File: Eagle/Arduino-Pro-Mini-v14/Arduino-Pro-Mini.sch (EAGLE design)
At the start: 15 parts, among them Q1 8/16/20MHz, U1 ATMEGA328, U2 MIC5205

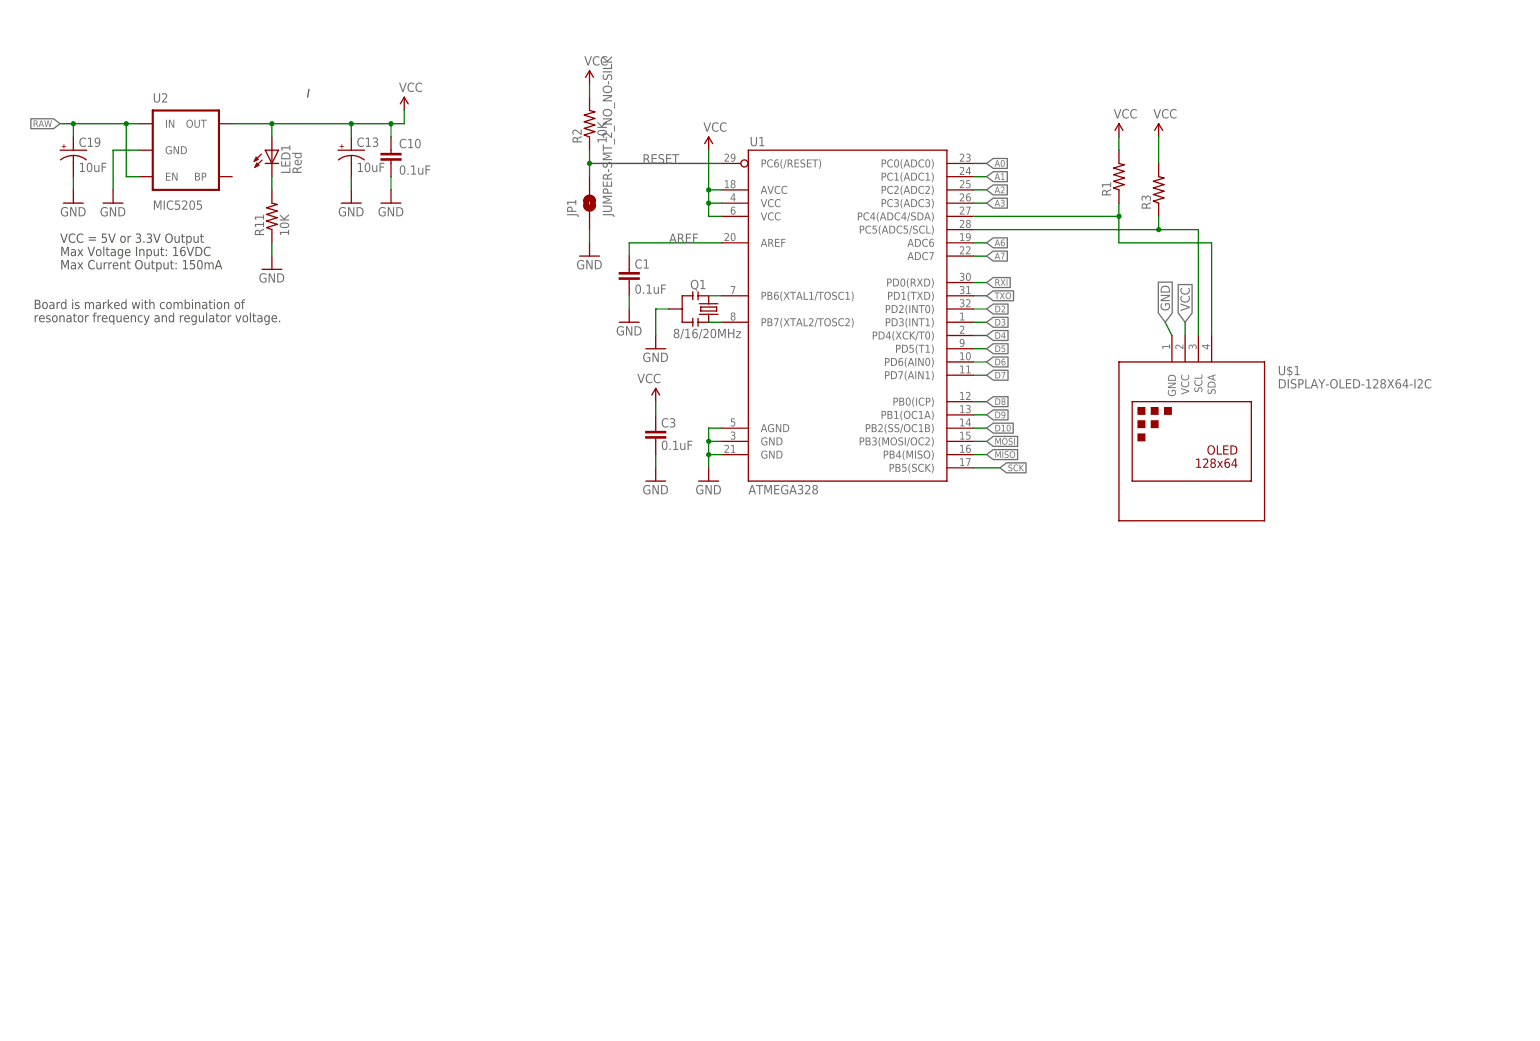
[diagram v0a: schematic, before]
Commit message: Added LED driers
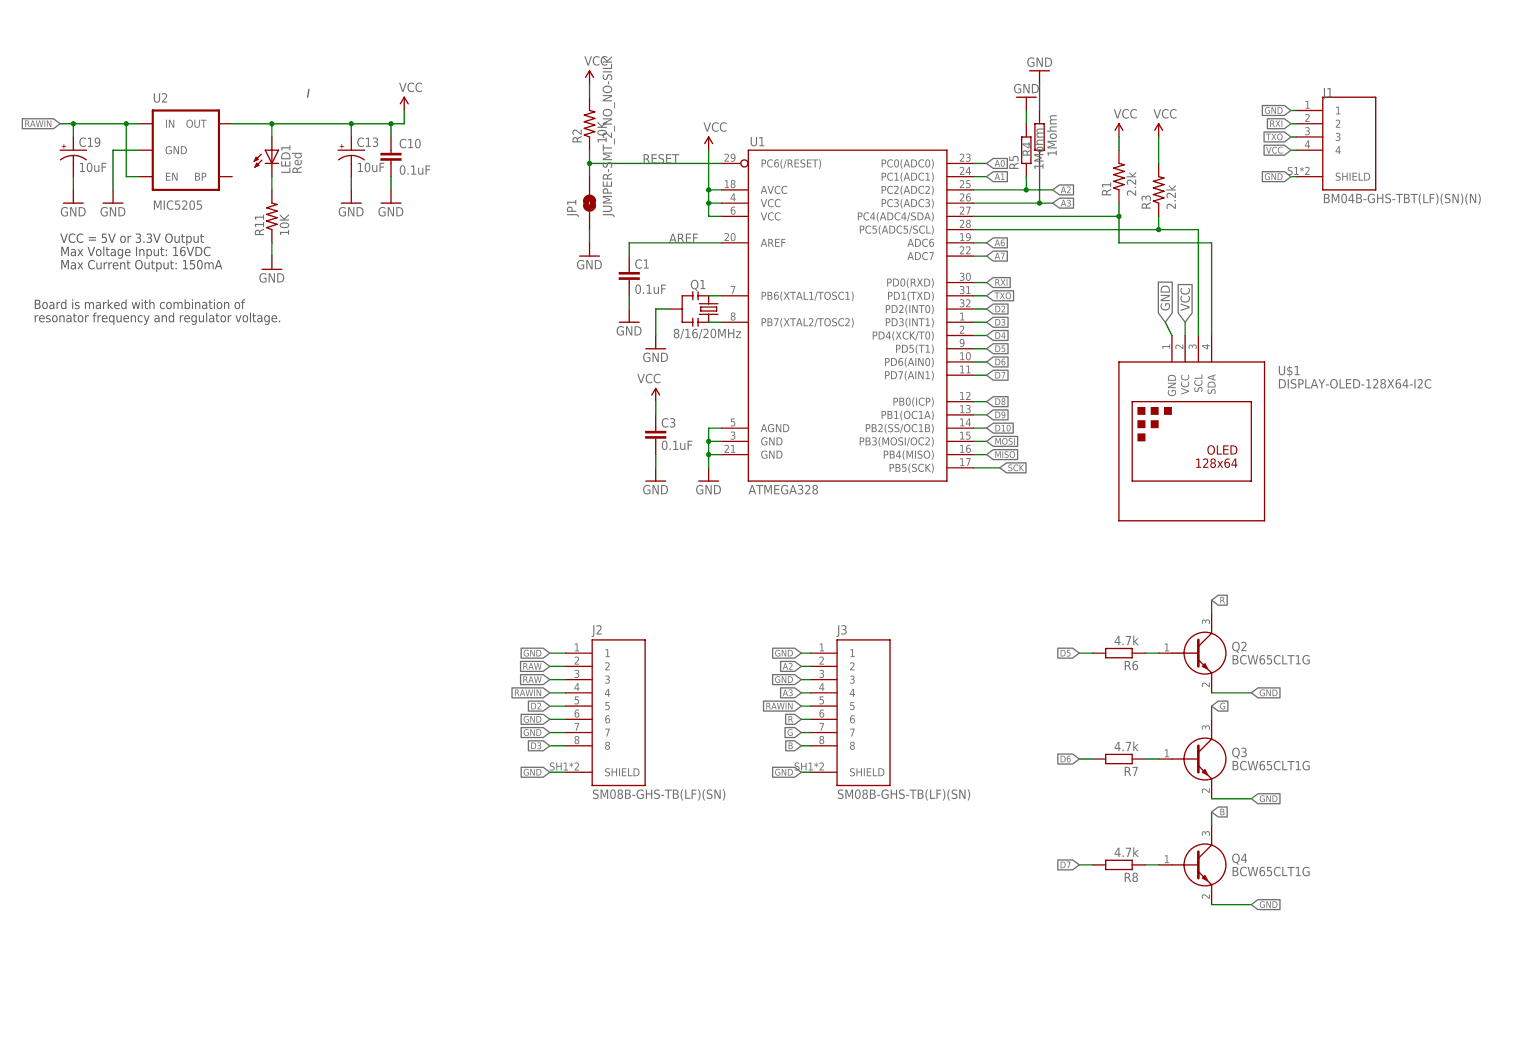
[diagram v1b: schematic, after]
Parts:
- added J1: BM04B-GHS-TBT(LF)(SN)(N), BM04B-GHS-TBT_LF__SN__N_:BM04B-GHS-TBT(LF)(SN)(N)
- added J2, J3: SM08B-GHS-TB(LF)(SN), SM08B-GHS-TB_LF__SN_:SM08B-GHS-TB(LF)(SN)
- added Q2, Q3, Q4: BCW65CLT1G, BCW65CLT1G:BCW65CLT1G
- added R4, R5: 1Mohm, eagle-ltspice:RR0402
- added R6, R7, R8: 4.7k, eagle-ltspice:RR0402
- R1, R3: value (none) -> 2.2k
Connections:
- new net B: J3.8, Q4.C
- new net G: J3.7, Q3.C
- new net N$3: Q4.B, R8.1
- new net N$5: Q3.B, R7.1
- new net N$6: Q2.B, R6.1
- new net R: J3.6, Q2.C
- new net RAWIN: C19.+, J2.4, J3.5, U2.EN, U2.IN
- net A2: now also J3.2, R5.1
- net A3: now also J3.4, R4.1
- net D2: now also J2.5
- net D3: now also J2.8
- net D5: now also R6.2
- net D6: now also R7.2
- net D7: now also R8.2
- net GND: now also J1.1, J1.SHIELD, J2.1, J2.6, J2.7, J2.SHIELD, J3.1, J3.3, J3.SHIELD, Q2.E, Q3.E, Q4.E, R4.2, R5.2
- net RAW: now also J2.2, J2.3; no longer C19.+, U2.EN, U2.IN
- net RXI: now also J1.2
- net TXO: now also J1.3
- net VCC: now also J1.4

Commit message: things
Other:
- note removed: "Board is marked with combination of"
- note removed: "Max Current Output: 150mA"
- note removed: "Max Voltage Input: 16VDC"
- note removed: "VCC = 5V or 3.3V Output"
- note removed: "resonator frequency and regulator voltage."
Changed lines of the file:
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@@
 <?xml version="1.0" encoding="utf-8"?>
 <!DOCTYPE eagle SYSTEM "eagle.dtd">
-<eagle version="9.2.2">
+<eagle version="9.5.1">
 <drawing>
 <settings>
@@
 <sheet>
 <plain>
-<text x="20.32" y="137.16" size="1.778" layer="97">Max Voltage Input: 16VDC</text>
-<text x="20.32" y="134.62" size="1.778" layer="97">Max Current Output: 150mA</text>
-<text x="15.24" y="127" size="1.778" layer="97">Board is marked with combination of</text>
-<text x="15.24" y="124.46" size="1.778" layer="97">resonator frequency and regulator voltage.</text>
-<text x="20.32" y="139.7" size="1.778" layer="97">VCC = 5V or 3.3V Output</text>
 <wire x1="67.818" y1="167.64" x2="68.072" y2="169.164" width="0.2032" layer="97"/>
 </plain>

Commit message: Auto stash before merge of "master" and "origin/master"
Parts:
- added R10, R12, R13, R9: 10ohm, eagle-ltspice:RR0402
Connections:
- new net N$7: Q4.C, R9.2
- new net N$8: Q3.C, R10.2
- new net N$9: Q2.C, R12.2
- net AREF: now also R13.2
- net B: now also R9.1; no longer Q4.C
- net G: now also R10.1; no longer Q3.C
- net R: now also R12.1; no longer Q2.C
- net VCC: now also R13.1
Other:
- moved on the sheet: Q3, Q4, R7, R8
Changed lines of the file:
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@@
 <part name="R7" library="eagle-ltspice" library_urn="urn:adsk.eagle:library:217" deviceset="R" device="R0402" package3d_urn="urn:adsk.eagle:package:13296/1" value="4.7k"/>
 <part name="R8" library="eagle-ltspice" library_urn="urn:adsk.eagle:library:217" deviceset="R" device="R0402" package3d_urn="urn:adsk.eagle:package:13296/1" value="4.7k"/>
+<part name="R9" library="eagle-ltspice" library_urn="urn:adsk.eagle:library:217" deviceset="R" device="R0402" package3d_urn="urn:adsk.eagle:package:13296/1" value="10ohm"/>
+<part name="R10" library="eagle-ltspice" library_urn="urn:adsk.eagle:library:217" deviceset="R" device="R0402" package3d_urn="urn:adsk.eagle:package:13296/1" value="10ohm"/>
+<part name="R12" library="eagle-ltspice" library_urn="urn:adsk.eagle:library:217" deviceset="R" device="R0402" package3d_urn="urn:adsk.eagle:package:13296/1" value="10ohm"/>
+<part name="R13" library="eagle-ltspice" library_urn="urn:adsk.eagle:library:217" deviceset="R" device="R0402" package3d_urn="urn:adsk.eagle:package:13296/1" value="10ohm"/>
 </parts>
 <sheets>
@@
 <attribute name="VALUE" x="245.11" y="59.69" size="1.778" layer="96" align="center-left"/>
 </instance>
-<instance part="Q3" gate="G$1" x="231.14" y="40.64" smashed="yes">
-<attribute name="NAME" x="245.11" y="41.91" size="1.778" layer="95" align="center-left"/>
-<attribute name="VALUE" x="245.11" y="39.37" size="1.778" layer="96" align="center-left"/>
-</instance>
-<instance part="Q4" gate="G$1" x="231.14" y="20.32" smashed="yes">
-<attribute name="NAME" x="245.11" y="21.59" size="1.778" layer="95" align="center-left"/>
-<attribute name="VALUE" x="245.11" y="19.05" size="1.778" layer="96" align="center-left"/>
+<instance part="Q3" gate="G$1" x="231.14" y="27.94" smashed="yes">
+<attribute name="NAME" x="245.11" y="29.21" size="1.778" layer="95" align="center-left"/>
+<attribute name="VALUE" x="245.11" y="26.67" size="1.778" layer="96" align="center-left"/>
+</instance>
+<instance part="Q4" gate="G$1" x="231.14" y="-2.54" smashed="yes">
+<attribute name="NAME" x="245.11" y="-1.27" size="1.778" layer="95" align="center-left"/>
+<attribute name="VALUE" x="245.11" y="-3.81" size="1.778" layer="96" align="center-left"/>
 </instance>
 <instance part="R6" gate="G$1" x="223.52" y="60.96" smashed="yes" rot="R180">
@@
 <attribute name="VALUE" x="227.33" y="64.262" size="1.778" layer="96" rot="R180"/>
 </instance>
-<instance part="R7" gate="G$1" x="223.52" y="40.64" smashed="yes" rot="R180">
-<attribute name="NAME" x="227.33" y="39.1414" size="1.778" layer="95" rot="R180"/>
-<attribute name="VALUE" x="227.33" y="43.942" size="1.778" layer="96" rot="R180"/>
-</instance>
-<instance part="R8" gate="G$1" x="223.52" y="20.32" smashed="yes" rot="R180">
-<attribute name="NAME" x="227.33" y="18.8214" size="1.778" layer="95" rot="R180"/>
-<attribute name="VALUE" x="227.33" y="23.622" size="1.778" layer="96" rot="R180"/>
+<instance part="R7" gate="G$1" x="223.52" y="27.94" smashed="yes" rot="R180">
+<attribute name="NAME" x="227.33" y="26.4414" size="1.778" layer="95" rot="R180"/>
+<attribute name="VALUE" x="227.33" y="31.242" size="1.778" layer="96" rot="R180"/>
+</instance>
+<instance part="R8" gate="G$1" x="223.52" y="-2.54" smashed="yes" rot="R180">
+<attribute name="NAME" x="227.33" y="-4.0386" size="1.778" layer="95" rot="R180"/>
+<attribute name="VALUE" x="227.33" y="0.762" size="1.778" layer="96" rot="R180"/>
+</instance>
+<instance part="R9" gate="G$1" x="241.3" y="10.16" smashed="yes" rot="R270">
+<attribute name="NAME" x="242.7986" y="13.97" size="1.778" layer="95" rot="R270"/>
+<attribute name="VALUE" x="237.998" y="13.97" size="1.778" layer="96" rot="R270"/>
+</instance>
+<instance part="R10" gate="G$1" x="241.3" y="40.64" smashed="yes" rot="R270">
+<attribute name="NAME" x="242.7986" y="44.45" size="1.778" layer="95" rot="R270"/>
+<attribute name="VALUE" x="237.998" y="44.45" size="1.778" layer="96" rot="R270"/>
+</instance>
+<instance part="R12" gate="G$1" x="241.3" y="73.66" smashed="yes" rot="R270">
+<attribute name="NAME" x="242.7986" y="77.47" size="1.778" layer="95" rot="R270"/>
+<attribute name="VALUE" x="237.998" y="77.47" size="1.778" layer="96" rot="R270"/>
+</instance>
+<instance part="R13" gate="G$1" x="134.62" y="144.78" smashed="yes" rot="R270">
+<attribute name="NAME" x="136.1186" y="148.59" size="1.778" layer="95" rot="R270"/>
+<attribute name="VALUE" x="131.318" y="148.59" size="1.778" layer="96" rot="R270"/>
 </instance>
 </instances>
@@
 <segment>
 <pinref part="Q3" gate="G$1" pin="E"/>
-<wire x1="241.3" y1="33.02" x2="248.92" y2="33.02" width="0.1524" layer="91"/>
-<label x="248.92" y="33.02" size="1.27" layer="95" xref="yes"/>
+<wire x1="241.3" y1="20.32" x2="248.92" y2="20.32" width="0.1524" layer="91"/>
+<label x="248.92" y="20.32" size="1.27" layer="95" xref="yes"/>
 </segment>
 <segment>
 <pinref part="Q4" gate="G$1" pin="E"/>
-<wire x1="241.3" y1="12.7" x2="248.92" y2="12.7" width="0.1524" layer="91"/>
-<label x="248.92" y="12.7" size="1.27" layer="95" xref="yes"/>
+<wire x1="241.3" y1="-10.16" x2="248.92" y2="-10.16" width="0.1524" layer="91"/>
+<label x="248.92" y="-10.16" size="1.27" layer="95" xref="yes"/>
 </segment>
 </net>
 <net name="AREF" class="0">
 <segment>
-<wire x1="147.32" y1="139.7" x2="129.54" y2="139.7" width="0.1524" layer="91"/>
+<wire x1="147.32" y1="139.7" x2="134.62" y2="139.7" width="0.1524" layer="91"/>
+<wire x1="134.62" y1="139.7" x2="129.54" y2="139.7" width="0.1524" layer="91"/>
 <wire x1="129.54" y1="139.7" x2="129.54" y2="137.16" width="0.1524" layer="91"/>
 <label x="137.16" y="139.7" size="1.778" layer="95"/>
 <pinref part="C1" gate="G$1" pin="2"/>
 <pinref part="U1" gate="G$1" pin="AREF"/>
+<pinref part="R13" gate="G$1" pin="2"/>
+<junction x="134.62" y="139.7"/>
 </segment>
 </net>
@@
 <segment>
 <wire x1="147.32" y1="149.86" x2="144.78" y2="149.86" width="0.1524" layer="91"/>
-<wire x1="144.78" y1="149.86" x2="144.78" y2="157.48" width="0.1524" layer="91"/>
+<wire x1="144.78" y1="149.86" x2="144.78" y2="152.4" width="0.1524" layer="91"/>
+<wire x1="144.78" y1="152.4" x2="144.78" y2="157.48" width="0.1524" layer="91"/>
 <wire x1="147.32" y1="147.32" x2="144.78" y2="147.32" width="0.1524" layer="91"/>
 <wire x1="144.78" y1="147.32" x2="144.78" y2="149.86" width="0.1524" layer="91"/>
@@
 <pinref part="U1" gate="G$1" pin="VCC@2"/>
 <pinref part="P+1" gate="G$1" pin="3.3V"/>
+<pinref part="R13" gate="G$1" pin="1"/>
+<wire x1="134.62" y1="149.86" x2="134.62" y2="152.4" width="0.1524" layer="91"/>
+<wire x1="134.62" y1="152.4" x2="144.78" y2="152.4" width="0.1524" layer="91"/>
+<junction x="144.78" y="152.4"/>
 </segment>
 <segment>
@@
 <segment>
 <pinref part="R7" gate="G$1" pin="2"/>
-<wire x1="218.44" y1="40.64" x2="215.9" y2="40.64" width="0.1524" layer="91"/>
-<label x="215.9" y="40.64" size="1.27" layer="95" rot="R180" xref="yes"/>
+<wire x1="218.44" y1="27.94" x2="215.9" y2="27.94" width="0.1524" layer="91"/>
+<label x="215.9" y="27.94" size="1.27" layer="95" rot="R180" xref="yes"/>
 </segment>
 </net>
@@
 <segment>
 <pinref part="R8" gate="G$1" pin="2"/>
-<wire x1="218.44" y1="20.32" x2="215.9" y2="20.32" width="0.1524" layer="91"/>
-<label x="215.9" y="20.32" size="1.27" layer="95" rot="R180" xref="yes"/>
+<wire x1="218.44" y1="-2.54" x2="215.9" y2="-2.54" width="0.1524" layer="91"/>
+<label x="215.9" y="-2.54" size="1.27" layer="95" rot="R180" xref="yes"/>
 </segment>
 </net>
@@
 </segment>
 <segment>
-<pinref part="Q4" gate="G$1" pin="C"/>
-<wire x1="241.3" y1="27.94" x2="241.3" y2="30.48" width="0.1524" layer="91"/>
-<label x="241.3" y="30.48" size="1.27" layer="95" xref="yes"/>
+<label x="241.3" y="17.78" size="1.27" layer="95" xref="yes"/>
+<wire x1="241.3" y1="15.24" x2="241.3" y2="17.78" width="0.1524" layer="91"/>
+<pinref part="R9" gate="G$1" pin="1"/>
 </segment>
 </net>
@@
 </segment>
 <segment>
-<pinref part="Q3" gate="G$1" pin="C"/>
-<wire x1="241.3" y1="48.26" x2="241.3" y2="50.8" width="0.1524" layer="91"/>
-<label x="241.3" y="50.8" size="1.27" layer="95" xref="yes"/>
+<label x="241.3" y="48.26" size="1.27" layer="95" xref="yes"/>
+<wire x1="241.3" y1="45.72" x2="241.3" y2="48.26" width="0.1524" layer="91"/>
+<pinref part="R10" gate="G$1" pin="1"/>
 </segment>
 </net>
@@
 </segment>
 <segment>
-<pinref part="Q2" gate="G$1" pin="C"/>
-<wire x1="241.3" y1="68.58" x2="241.3" y2="71.12" width="0.1524" layer="91"/>
-<label x="241.3" y="71.12" size="1.27" layer="95" xref="yes"/>
+<label x="241.3" y="81.28" size="1.27" layer="95" xref="yes"/>
+<pinref part="R12" gate="G$1" pin="1"/>
+<wire x1="241.3" y1="78.74" x2="241.3" y2="81.28" width="0.1524" layer="91"/>
 </segment>
 </net>
@@
 <pinref part="R8" gate="G$1" pin="1"/>
 <pinref part="Q4" gate="G$1" pin="B"/>
-<wire x1="228.6" y1="20.32" x2="231.14" y2="20.32" width="0.1524" layer="91"/>
+<wire x1="228.6" y1="-2.54" x2="231.14" y2="-2.54" width="0.1524" layer="91"/>
 </segment>
 </net>
@@
 <pinref part="Q3" gate="G$1" pin="B"/>
 <pinref part="R7" gate="G$1" pin="1"/>
-<wire x1="231.14" y1="40.64" x2="228.6" y2="40.64" width="0.1524" layer="91"/>
+<wire x1="231.14" y1="27.94" x2="228.6" y2="27.94" width="0.1524" layer="91"/>
 </segment>
 </net>
@@
 </segment>
 </net>
+<net name="N$7" class="0">
+<segment>
+<pinref part="Q4" gate="G$1" pin="C"/>
+<pinref part="R9" gate="G$1" pin="2"/>
+</segment>
+</net>
+<net name="N$8" class="0">
+<segment>
+<pinref part="Q3" gate="G$1" pin="C"/>
+<pinref part="R10" gate="G$1" pin="2"/>
+</segment>
+</net>
+<net name="N$9" class="0">
+<segment>
+<pinref part="Q2" gate="G$1" pin="C"/>
+<pinref part="R12" gate="G$1" pin="2"/>
+</segment>
+</net>
